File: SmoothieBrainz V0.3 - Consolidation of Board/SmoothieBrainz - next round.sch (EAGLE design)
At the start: 220 parts, among them IC1 LPC1769, IC5 LD117ADT33TR, Q1 BSL207SP, Q2 12MHz, SW1 SW_TACT_4P_B, SW3 SW_TACT_4P_B, U3 USD-SOCKETUSD, X1 MSTBA2, X14 USBPTH, X2 GMSTBA2, X3 GMSTBA4, X4 1751248, X5 1751248, X6 1751248, X7 1751248

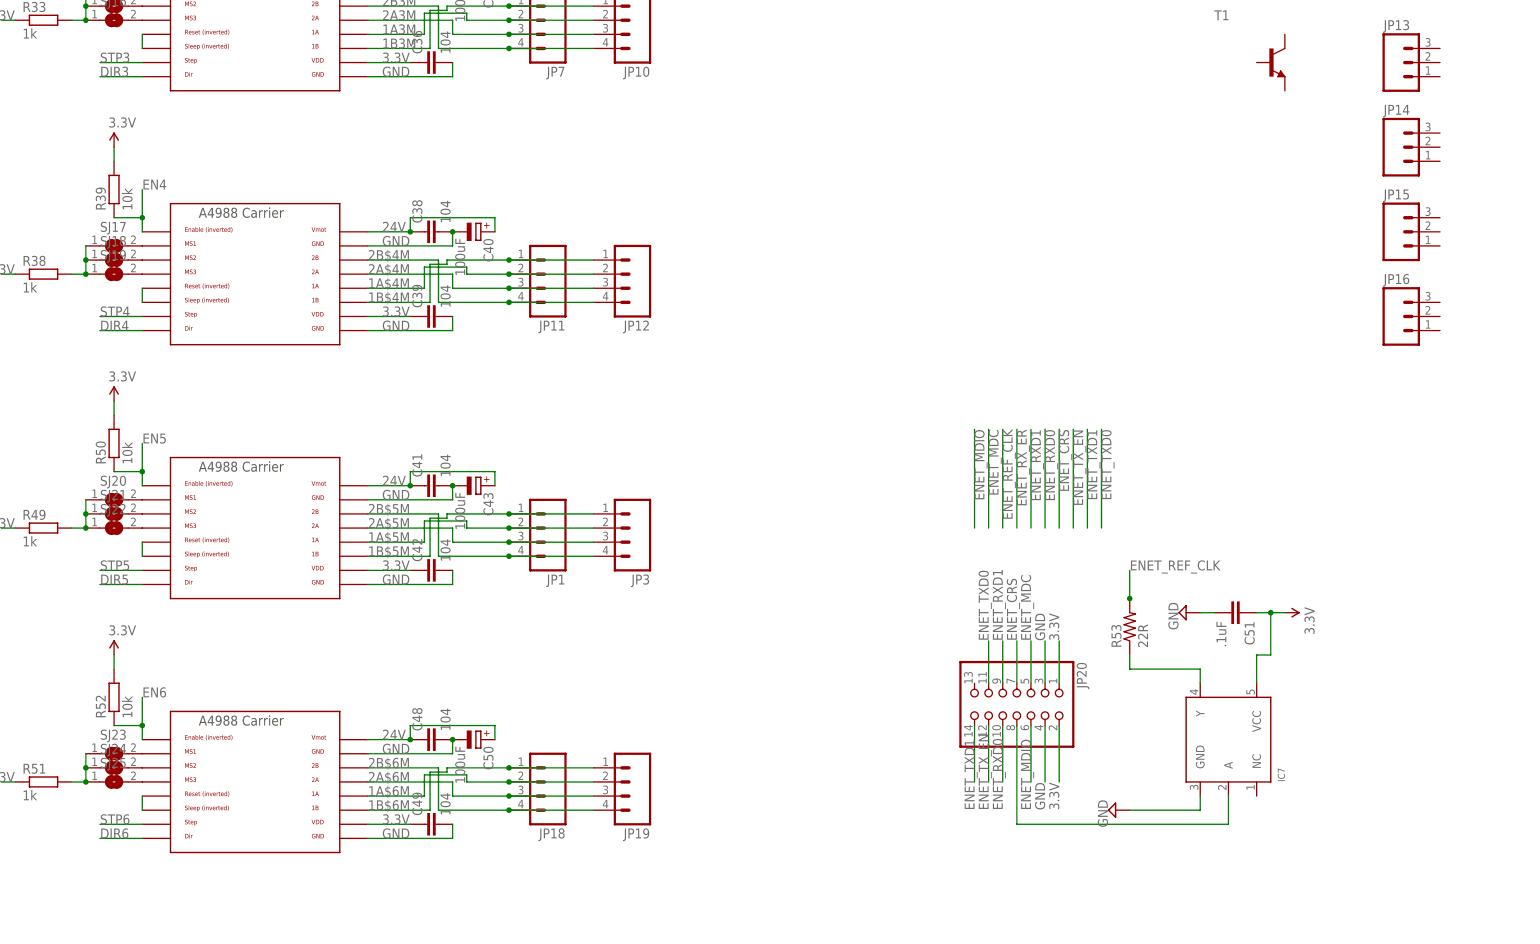
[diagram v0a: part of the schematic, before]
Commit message: mosfet #6 added to board
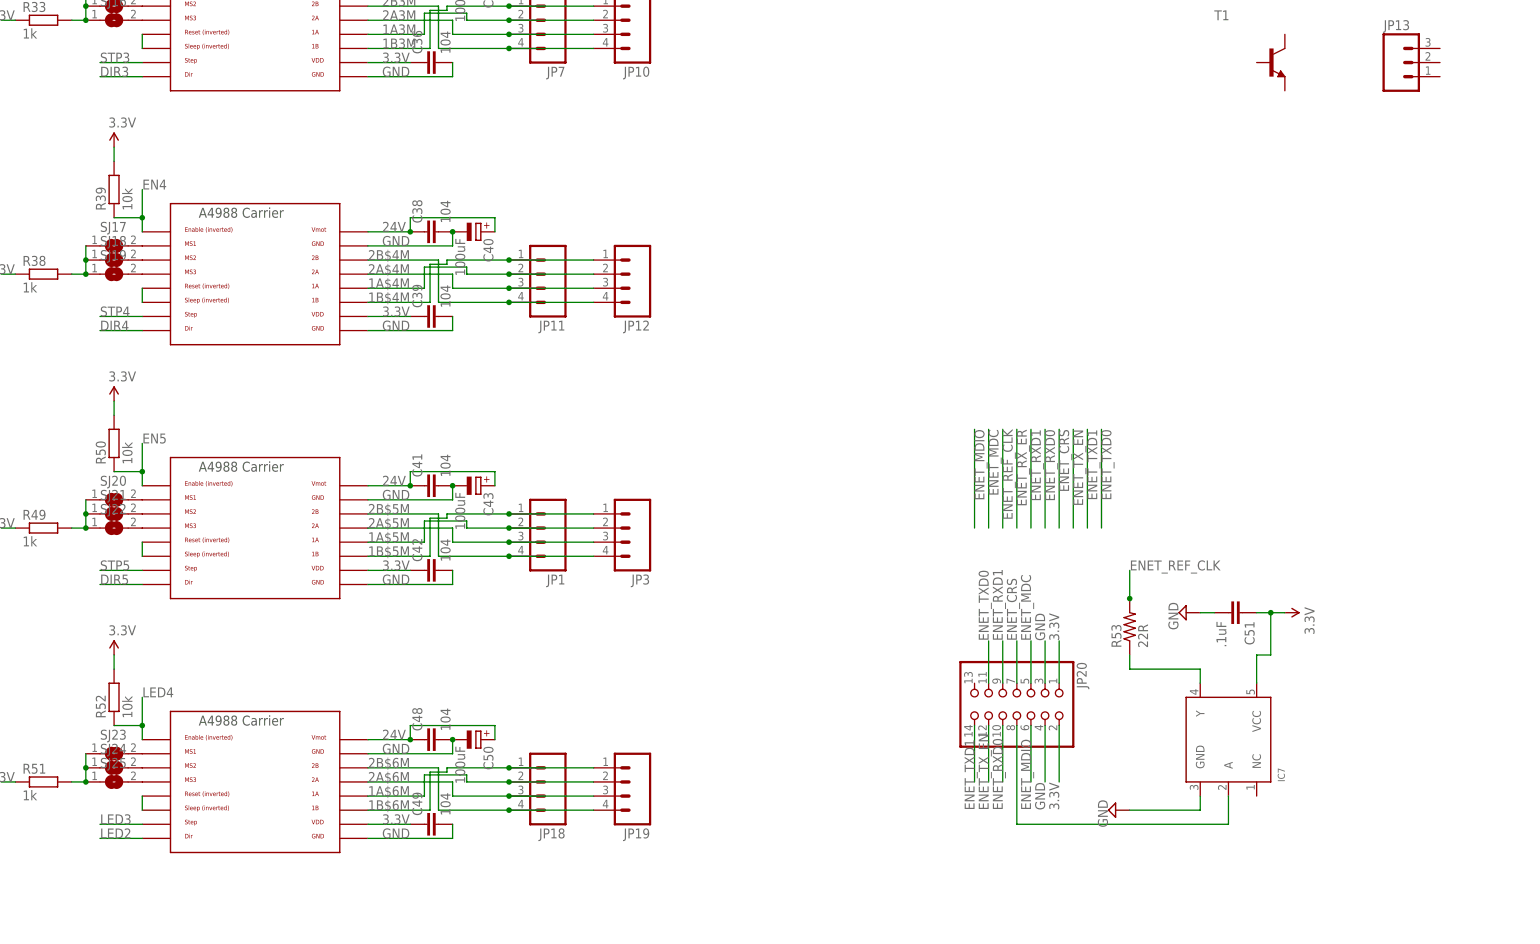
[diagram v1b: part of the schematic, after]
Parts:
- removed JP14, JP15, JP16: (no value), SparkFun-Connectors:M03LOCK
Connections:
- removed net DIR6: U$9.DIR
- removed net EN6: R52.1, U$9.EN
- removed net STP6: U$9.STEP
- net LED2: now also U$9.DIR
- net LED3: now also U$9.STEP
- net LED4: now also R52.1, U$9.EN
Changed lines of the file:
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@@
 <part name="T1" library="transistor" deviceset="*-NPN-" device="SOT23-BEC" technology="BC817-40"/>
 <part name="JP13" library="SparkFun-Connectors" deviceset="M03" device="LOCK"/>
-<part name="JP14" library="SparkFun-Connectors" deviceset="M03" device="LOCK"/>
-<part name="JP15" library="SparkFun-Connectors" deviceset="M03" device="LOCK"/>
-<part name="JP16" library="SparkFun-Connectors" deviceset="M03" device="LOCK"/>
 <part name="X1" library="con-phoenix-508" deviceset="MSTBA2" device=""/>
 <part name="D5" library="semicon-smd-ipc" deviceset="D-" device="SOD-87" value="M4"/>
@@
 <instance part="T1" gate="G$1" x="525.78" y="157.48"/>
 <instance part="JP13" gate="G$1" x="548.64" y="157.48"/>
-<instance part="JP14" gate="G$1" x="548.64" y="142.24"/>
-<instance part="JP15" gate="G$1" x="548.64" y="127"/>
-<instance part="JP16" gate="G$1" x="548.64" y="111.76"/>
 <instance part="X1" gate="-1" x="515.62" y="187.96"/>
 <instance part="X1" gate="-2" x="515.62" y="177.8"/>
@@
 <pinref part="IC1" gate="G$1" pin="P1[19]/MC0A/USB_PPWR/CAP1[1]"/>
 </segment>
+<segment>
+<pinref part="U$9" gate="G$1" pin="DIR"/>
+<wire x1="322.58" y1="17.78" x2="314.96" y2="17.78" width="0.1524" layer="91"/>
+<label x="314.96" y="17.78" size="1.778" layer="95"/>
+</segment>
 </net>
 <net name="LED3" class="0">
@@
 <pinref part="IC1" gate="G$1" pin="P1[20]/MCFB0/PWM1[2]/SCK0"/>
 </segment>
+<segment>
+<pinref part="U$9" gate="G$1" pin="STEP"/>
+<wire x1="322.58" y1="20.32" x2="314.96" y2="20.32" width="0.1524" layer="91"/>
+<label x="314.96" y="20.32" size="1.778" layer="95"/>
+</segment>
 </net>
 <net name="LED4" class="0">
@@
 <pinref part="IC1" gate="G$1" pin="P1[21]/MCABORT/PWM1[3]/SSEL0"/>
 </segment>
+<segment>
+<pinref part="U$9" gate="G$1" pin="EN"/>
+<wire x1="322.58" y1="35.56" x2="322.58" y2="38.1" width="0.1524" layer="91"/>
+<label x="322.58" y="43.18" size="1.778" layer="95"/>
+<pinref part="R52" gate="G$1" pin="1"/>
+<wire x1="322.58" y1="38.1" x2="322.58" y2="43.18" width="0.1524" layer="91"/>
+<wire x1="317.5" y1="38.1" x2="322.58" y2="38.1" width="0.1524" layer="91"/>
+<junction x="322.58" y="38.1"/>
+</segment>
 </net>
 <net name="TH4" class="0">
@@
 </segment>
 </net>
-<net name="EN6" class="0">
-<segment>
-<pinref part="U$9" gate="G$1" pin="EN"/>
-<wire x1="322.58" y1="35.56" x2="322.58" y2="38.1" width="0.1524" layer="91"/>
-<label x="322.58" y="43.18" size="1.778" layer="95"/>
-<pinref part="R52" gate="G$1" pin="1"/>
-<wire x1="322.58" y1="38.1" x2="322.58" y2="43.18" width="0.1524" layer="91"/>
-<wire x1="317.5" y1="38.1" x2="322.58" y2="38.1" width="0.1524" layer="91"/>
-<junction x="322.58" y="38.1"/>
-</segment>
-</net>
-<net name="STP6" class="0">
-<segment>
-<pinref part="U$9" gate="G$1" pin="STEP"/>
-<wire x1="322.58" y1="20.32" x2="314.96" y2="20.32" width="0.1524" layer="91"/>
-<label x="314.96" y="20.32" size="1.778" layer="95"/>
-</segment>
-</net>
-<net name="DIR6" class="0">
-<segment>
-<pinref part="U$9" gate="G$1" pin="DIR"/>
-<wire x1="322.58" y1="17.78" x2="314.96" y2="17.78" width="0.1524" layer="91"/>
-<label x="314.96" y="17.78" size="1.778" layer="95"/>
-</segment>
-</net>

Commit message: mosfet6 circuit complete, lots more routing
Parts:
- added R54: 10r, resistor:R-EU_R0603
- added R55: 100k, resistor:R-EU_R0603
- C28: value .1uF -> 104
- RN2: value (none) -> 4k7
- T1: value (none) -> BC817
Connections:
- new net N$55: R54.2, T1.B
- new net N$56: JP13.2, T1.C
- net 24V: now also JP13.1
- net 5V: now also JP13.3
- net GND: now also R55.1, T1.E
- net LED1: now also R54.1, R55.2
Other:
- moved on the sheet: JP13, T1
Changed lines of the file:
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@@
 <part name="R4" library="adafruit" deviceset="R-US_" device="R0603" value="10K"/>
 <part name="R16" library="adafruit" deviceset="R-US_" device="R0603" value="10K"/>
-<part name="C28" library="resistor" deviceset="C-EU" device="C0603" value=".1uF"/>
+<part name="C28" library="resistor" deviceset="C-EU" device="C0603" value="104"/>
 <part name="SJ2" library="SparkFun-Retired" deviceset="SOLDERJUMPER" device="NC" value="SOLDERJUMPERNC"/>
 <part name="SJ3" library="SparkFun-Retired" deviceset="SOLDERJUMPER" device="NC" value="SOLDERJUMPERNC"/>
@@
 <part name="U1" library="SparkFun-PowerIC" deviceset="V_REG_LM1117" device="SOT223"/>
 <part name="SUPPLY5" library="supply2" deviceset="GND" device=""/>
-<part name="RN2" library="resistor-dil" deviceset="4R-N" device="0603-ARV"/>
+<part name="RN2" library="resistor-dil" deviceset="4R-N" device="0603-ARV" value="4k7"/>
 <part name="U$14" library="Cohesion_parts" deviceset="N-POWER-MOSFET" device="DPAK-MOSFET" value="IRLR024"/>
 <part name="R40" library="resistor" deviceset="R-EU_" device="R0603" value="10r"/>
@@
 <part name="P+9" library="SparkFun" deviceset="3.3V" device=""/>
 <part name="JP3" library="SparkFun-Connectors" deviceset="M04" device="LOCK"/>
-<part name="T1" library="transistor" deviceset="*-NPN-" device="SOT23-BEC" technology="BC817-40"/>
+<part name="T1" library="transistor" deviceset="*-NPN-" device="SOT23-BEC" technology="BC817-40" value="BC817"/>
 <part name="JP13" library="SparkFun-Connectors" deviceset="M03" device="LOCK"/>
 <part name="X1" library="con-phoenix-508" deviceset="MSTBA2" device=""/>
@@
 <part name="SUPPLY57" library="supply2" deviceset="GND" device=""/>
 <part name="P+18" library="SparkFun" deviceset="3.3V" device=""/>
+<part name="GND4" library="supply1" deviceset="GND" device=""/>
+<part name="R54" library="resistor" deviceset="R-EU_" device="R0603" value="10r"/>
+<part name="R55" library="resistor" deviceset="R-EU_" device="R0603" value="100k"/>
 </parts>
 <sheets>
@@
 <instance part="P+9" gate="G$1" x="317.5" y="96.52"/>
 <instance part="JP3" gate="G$1" x="408.94" y="73.66" rot="R180"/>
-<instance part="T1" gate="G$1" x="525.78" y="157.48"/>
-<instance part="JP13" gate="G$1" x="548.64" y="157.48"/>
+<instance part="T1" gate="G$1" x="515.62" y="137.16"/>
+<instance part="JP13" gate="G$1" x="543.56" y="149.86" rot="R180"/>
 <instance part="X1" gate="-1" x="515.62" y="187.96"/>
 <instance part="X1" gate="-2" x="515.62" y="177.8"/>
@@
 <instance part="SUPPLY57" gate="GND" x="510.54" y="58.42" rot="R270"/>
 <instance part="P+18" gate="G$1" x="528.32" y="58.42" rot="R270"/>
+<instance part="GND4" gate="1" x="518.16" y="121.92"/>
+<instance part="R54" gate="G$1" x="505.46" y="137.16"/>
+<instance part="R55" gate="G$1" x="510.54" y="129.54" rot="R180"/>
 </instances>
 <busses>
@@
 <pinref part="C51" gate="G$1" pin="2"/>
 </segment>
+<segment>
+<pinref part="GND4" gate="1" pin="GND"/>
+<pinref part="T1" gate="G$1" pin="E"/>
+<wire x1="518.16" y1="124.46" x2="518.16" y2="129.54" width="0.1524" layer="91"/>
+<pinref part="R55" gate="G$1" pin="1"/>
+<wire x1="518.16" y1="129.54" x2="518.16" y2="132.08" width="0.1524" layer="91"/>
+<wire x1="515.62" y1="129.54" x2="518.16" y2="129.54" width="0.1524" layer="91"/>
+<junction x="518.16" y="129.54"/>
+</segment>
 </net>
 <net name="3.3V" class="0">
@@
 <pinref part="IC1" gate="G$1" pin="P1[18]/USB_UP_LED/PWM1[1]/CAP1[0]"/>
 </segment>
+<segment>
+<pinref part="R54" gate="G$1" pin="1"/>
+<wire x1="500.38" y1="137.16" x2="497.84" y2="137.16" width="0.1524" layer="91"/>
+<pinref part="R55" gate="G$1" pin="2"/>
+<wire x1="497.84" y1="137.16" x2="469.9" y2="137.16" width="0.1524" layer="91"/>
+<wire x1="505.46" y1="129.54" x2="497.84" y2="129.54" width="0.1524" layer="91"/>
+<wire x1="497.84" y1="129.54" x2="497.84" y2="137.16" width="0.1524" layer="91"/>
+<junction x="497.84" y="137.16"/>
+<label x="469.9" y="137.16" size="1.778" layer="95"/>
+</segment>
 </net>
 <net name="LED2" class="0">
@@
 <label x="25.4" y="-17.78" size="1.778" layer="95"/>
 </segment>
+<segment>
+<pinref part="JP13" gate="G$1" pin="3"/>
+<wire x1="535.94" y1="147.32" x2="525.78" y2="147.32" width="0.1524" layer="91"/>
+<label x="525.78" y="144.78" size="1.778" layer="95"/>
+</segment>
 </net>
 <net name="N$51" class="0">
@@
 <junction x="370.84" y="35.56"/>
 </segment>
+<segment>
+<pinref part="JP13" gate="G$1" pin="1"/>
+<wire x1="535.94" y1="152.4" x2="525.78" y2="152.4" width="0.1524" layer="91"/>
+<label x="525.78" y="152.4" size="1.778" layer="95"/>
+</segment>
 </net>
 <net name="N$16" class="0">
@@
 </segment>
 </net>
+<net name="N$55" class="0">
+<segment>
+<pinref part="R54" gate="G$1" pin="2"/>
+<wire x1="510.54" y1="137.16" x2="513.08" y2="137.16" width="0.1524" layer="91"/>
+<pinref part="T1" gate="G$1" pin="B"/>
+</segment>
+</net>
+<net name="N$56" class="0">
+<segment>
+<pinref part="T1" gate="G$1" pin="C"/>
+<wire x1="518.16" y1="142.24" x2="518.16" y2="144.78" width="0.1524" layer="91"/>
+<pinref part="JP13" gate="G$1" pin="2"/>
+<wire x1="518.16" y1="144.78" x2="518.16" y2="147.32" width="0.1524" layer="91"/>
+<wire x1="535.94" y1="149.86" x2="518.16" y2="149.86" width="0.1524" layer="91"/>
+<wire x1="518.16" y1="149.86" x2="518.16" y2="147.32" width="0.1524" layer="91"/>
+</segment>
+</net>

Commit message: BOM-0
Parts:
- removed U$11: FIDUCIAL, adafruit:FIDUCIAL
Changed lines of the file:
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@@
 <part name="JP9" library="SparkFun-Connectors" deviceset="M04" device="LOCK"/>
 <part name="JP10" library="SparkFun-Connectors" deviceset="M04" device="LOCK"/>
-<part name="U$11" library="adafruit" deviceset="FIDUCIAL" device=""/>
 <part name="U$12" library="adafruit" deviceset="FIDUCIAL" device=""/>
 <part name="U$13" library="Cohesion_parts" deviceset="N-POWER-MOSFET" device="DPAK-MOSFET" value="IRLR024"/>
@@
 <instance part="JP9" gate="G$1" x="408.94" y="208.28" rot="R180"/>
 <instance part="JP10" gate="G$1" x="408.94" y="165.1" rot="R180"/>
-<instance part="U$11" gate="G$1" x="17.78" y="215.9"/>
 <instance part="U$12" gate="G$1" x="27.94" y="215.9"/>
 <instance part="U$13" gate="G$1" x="528.32" y="335.28"/>

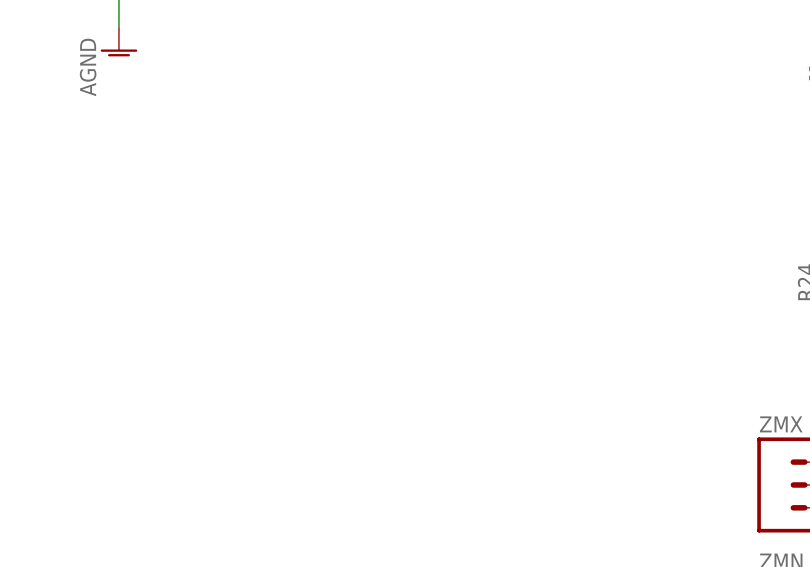
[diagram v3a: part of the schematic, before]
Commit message: major routing complete
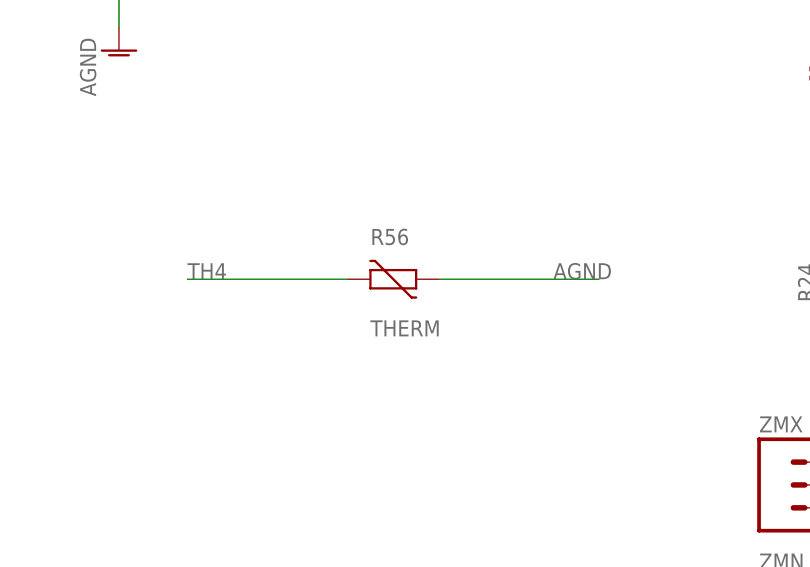
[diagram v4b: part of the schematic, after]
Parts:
- added R56: THERM, varistor:VARISTORCN0603
- LED10, LED11, LED6, LED7, LED8: device led:LEDSML0805 -> led:LEDSML0603
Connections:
- net AGND: now also R56.1
- net TH4: now also R56.2
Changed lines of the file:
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@@
 <part name="R30" library="resistor" deviceset="R-EU_" device="R0603" value="100k"/>
 <part name="R32" library="resistor" deviceset="R-EU_" device="R0603" value="1.5k"/>
-<part name="LED6" library="led" deviceset="LED" device="SML0805"/>
+<part name="LED6" library="led" deviceset="LED" device="SML0603"/>
 <part name="X2" library="con-phoenix-762" deviceset="GMSTBA2" device=""/>
 <part name="X3" library="con-phoenix-762" deviceset="GMSTBA4" device=""/>
@@
 <part name="R36" library="resistor" deviceset="R-EU_" device="R0603" value="100k"/>
 <part name="GND15" library="supply1" deviceset="GND" device=""/>
-<part name="LED7" library="led" deviceset="LED" device="SML0805"/>
+<part name="LED7" library="led" deviceset="LED" device="SML0603"/>
 <part name="R37" library="resistor" deviceset="R-EU_" device="R0603" value="1.5k"/>
 <part name="X4" library="con-phoenix-350" deviceset="1751248" device=""/>
@@
 <part name="R41" library="resistor" deviceset="R-EU_" device="R0603" value="100k"/>
 <part name="GND1" library="supply1" deviceset="GND" device=""/>
-<part name="LED8" library="led" deviceset="LED" device="SML0805"/>
+<part name="LED8" library="led" deviceset="LED" device="SML0603"/>
 <part name="R42" library="resistor" deviceset="R-EU_" device="R0603" value="1.5k"/>
 <part name="U$15" library="Cohesion_parts" deviceset="N-POWER-MOSFET" device="DPAK-MOSFET" value="IRLR024"/>
@@
 <part name="R44" library="resistor" deviceset="R-EU_" device="R0603" value="100k"/>
 <part name="GND2" library="supply1" deviceset="GND" device=""/>
-<part name="LED10" library="led" deviceset="LED" device="SML0805"/>
+<part name="LED10" library="led" deviceset="LED" device="SML0603"/>
 <part name="R45" library="resistor" deviceset="R-EU_" device="R0603" value="1.5k"/>
 <part name="U$16" library="Cohesion_parts" deviceset="N-POWER-MOSFET" device="DPAK-MOSFET" value="IRLR024"/>
@@
 <part name="R47" library="resistor" deviceset="R-EU_" device="R0603" value="100k"/>
 <part name="GND3" library="supply1" deviceset="GND" device=""/>
-<part name="LED11" library="led" deviceset="LED" device="SML0805"/>
+<part name="LED11" library="led" deviceset="LED" device="SML0603"/>
 <part name="R48" library="resistor" deviceset="R-EU_" device="R0603" value="1.5k"/>
 <part name="U$8" library="RepRapjr" deviceset="POLOLU_A4983CARRIER" device=""/>
@@
 <part name="R54" library="resistor" deviceset="R-EU_" device="R0603" value="10r"/>
 <part name="R55" library="resistor" deviceset="R-EU_" device="R0603" value="100k"/>
+<part name="R56" library="varistor" deviceset="VARISTOR" device="CN0603" value="THERM"/>
 </parts>
 <sheets>
@@
 <instance part="R54" gate="G$1" x="505.46" y="137.16"/>
 <instance part="R55" gate="G$1" x="510.54" y="129.54" rot="R180"/>
+<instance part="R56" gate="G$1" x="157.48" y="353.06"/>
 </instances>
 <busses>
@@
 <wire x1="144.78" y1="408.94" x2="182.88" y2="408.94" width="0.1524" layer="91"/>
 <junction x="182.88" y="408.94"/>
+</segment>
+<segment>
+<pinref part="R56" gate="G$1" pin="2"/>
+<wire x1="152.4" y1="353.06" x2="134.62" y2="353.06" width="0.1524" layer="91"/>
+<label x="134.62" y="353.06" size="1.778" layer="95"/>
 </segment>
 </net>
@@
 <junction x="172.72" y="386.08"/>
 </segment>
-</net>
+<segment>
+<pinref part="R56" gate="G$1" pin="1"/>
+<wire x1="162.56" y1="353.06" x2="180.34" y2="353.06" width="0.1524" layer="91"/>
+<label x="175.26" y="353.06" size="1.778" layer="95"/>
+</segment>
+</net>
